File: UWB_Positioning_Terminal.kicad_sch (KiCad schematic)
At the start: 0 parts

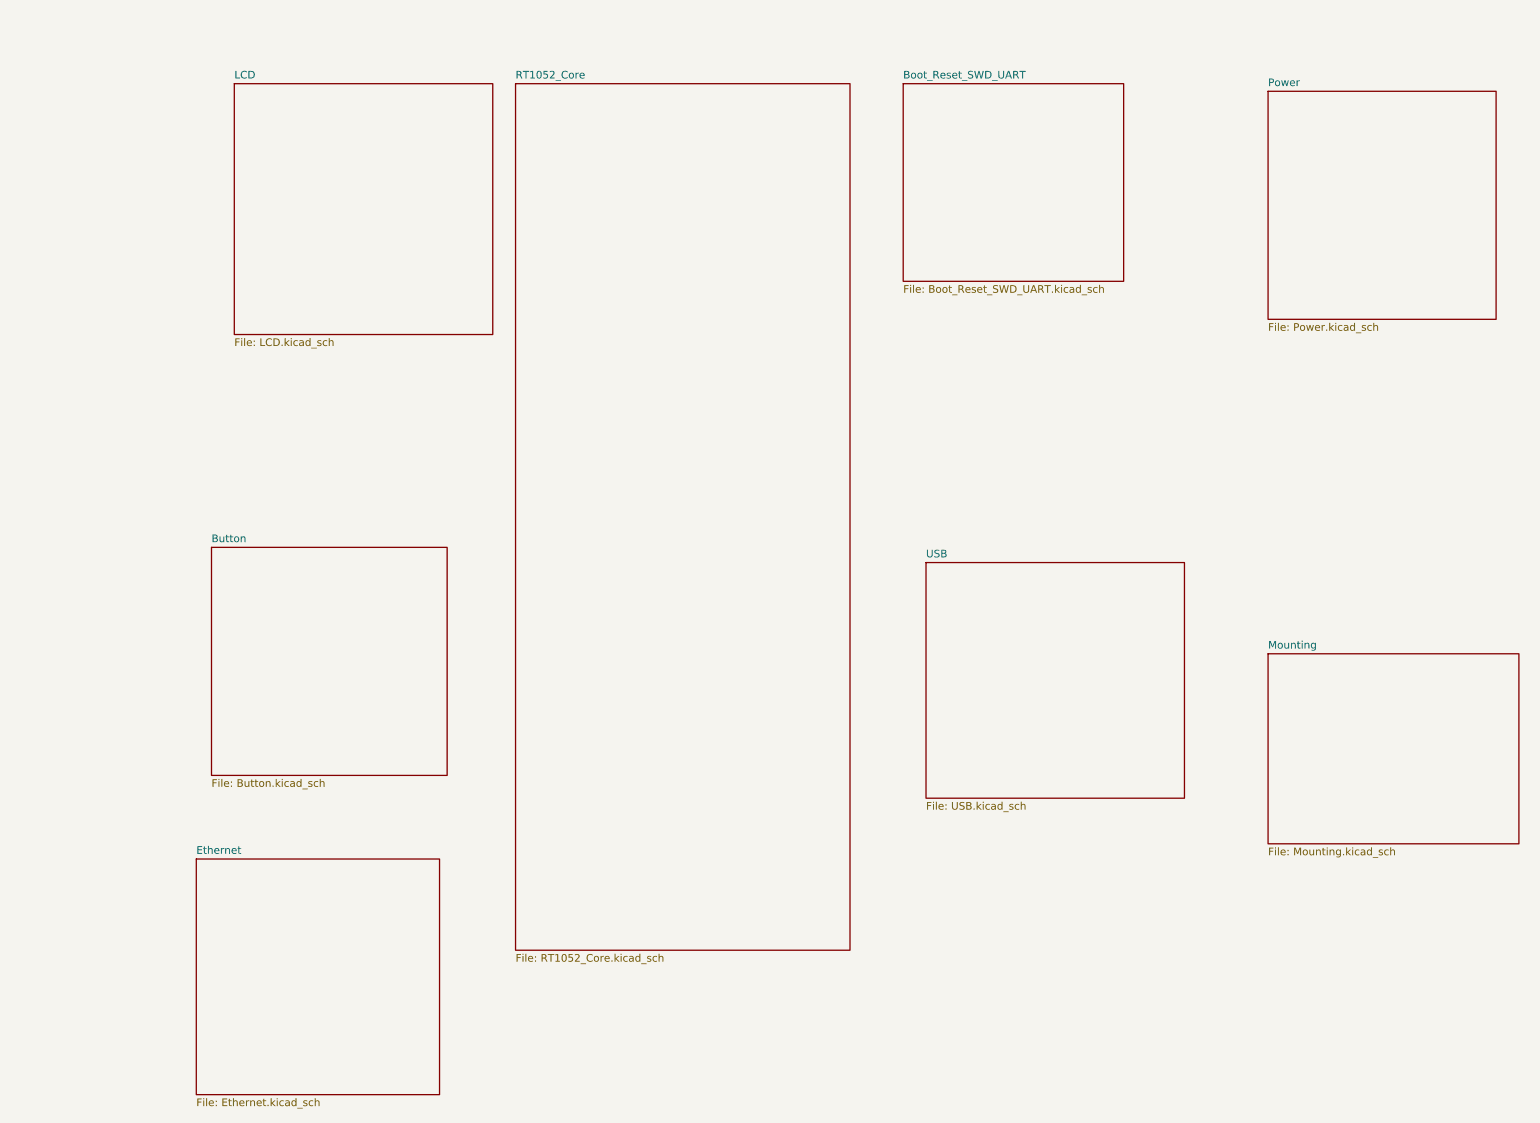
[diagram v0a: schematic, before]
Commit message: 2026 08 16 原理图完成，下一步制作分配未完成的器件封装，准备layout
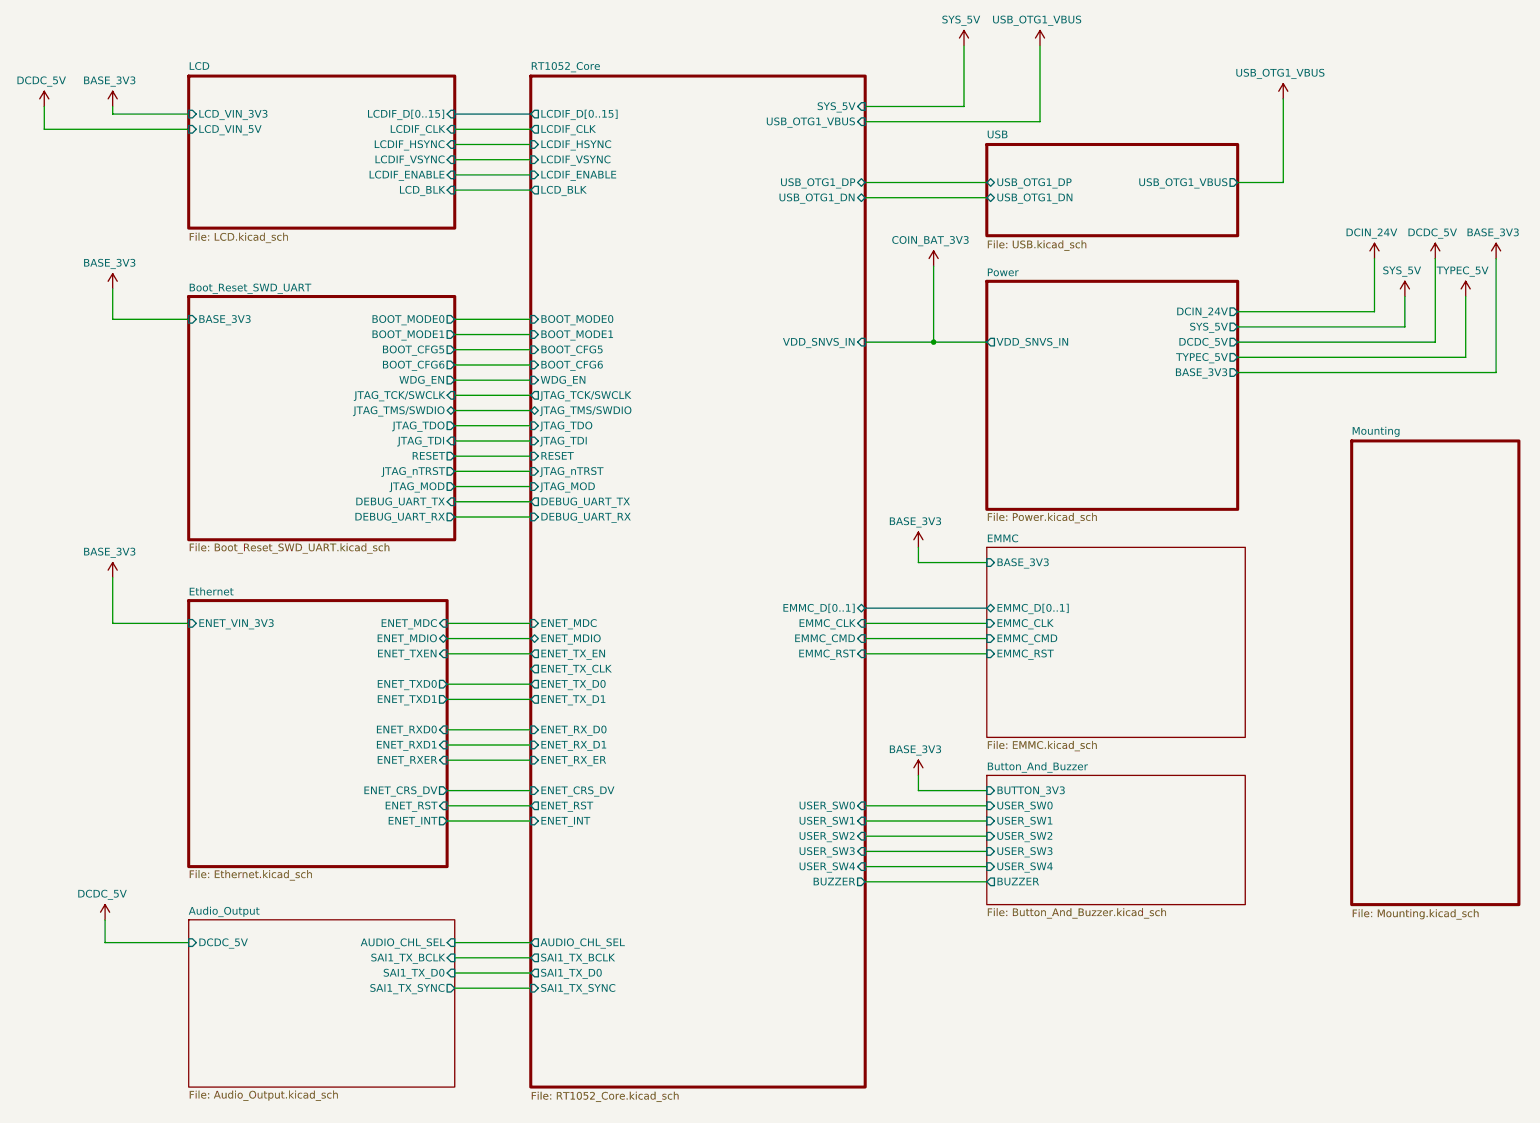
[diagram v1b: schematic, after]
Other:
- removed sheet Button
- added sheet Audio_Output (Audio_Output.kicad_sch)
- added sheet Button_And_Buzzer (Button_And_Buzzer.kicad_sch)
- added sheet EMMC (EMMC.kicad_sch)
- sheet Boot_Reset_SWD_UART ports: added BASE_3V3, BOOT_CFG5, BOOT_CFG6, BOOT_MODE0, BOOT_MODE1, DEBUG_UART_RX, DEBUG_UART_TX, JTAG_MOD, JTAG_TCK/SWCLK, JTAG_TDI, JTAG_TDO, JTAG_TMS/SWDIO, JTAG_nTRST, RESET, WDG_EN; removed none
- sheet Ethernet ports: added ENET_CRS_DV, ENET_INT, ENET_MDC, ENET_MDIO, ENET_RST, ENET_RXD0, ENET_RXD1, ENET_RXER, ENET_TXD0, ENET_TXD1, ENET_TXEN, ENET_VIN_3V3; removed none
- sheet LCD ports: added LCDIF_CLK, LCDIF_D[0..15], LCDIF_ENABLE, LCDIF_HSYNC, LCDIF_VSYNC, LCD_BLK, LCD_VIN_3V3, LCD_VIN_5V; removed none
- sheet Power ports: added BASE_3V3, DCDC_5V, DCIN_24V, SYS_5V, TYPEC_5V, VDD_SNVS_IN; removed none
- sheet RT1052_Core ports: added AUDIO_CHL_SEL, BOOT_CFG5, BOOT_CFG6, BOOT_MODE0, BOOT_MODE1, BUZZER, DEBUG_UART_RX, DEBUG_UART_TX, EMMC_CLK, EMMC_CMD, EMMC_D[0..1], EMMC_RST, ENET_CRS_DV, ENET_INT, ENET_MDC, ENET_MDIO, ENET_RST, ENET_RX_D0, ENET_RX_D1, ENET_RX_ER, ENET_TX_CLK, ENET_TX_D0, ENET_TX_D1, ENET_TX_EN, JTAG_MOD, JTAG_TCK/SWCLK, JTAG_TDI, JTAG_TDO, JTAG_TMS/SWDIO, JTAG_nTRST, LCDIF_CLK, LCDIF_D[0..15], LCDIF_ENABLE, LCDIF_HSYNC, LCDIF_VSYNC, LCD_BLK, RESET, SAI1_TX_BCLK, SAI1_TX_D0, SAI1_TX_SYNC, SYS_5V, USB_OTG1_DN, USB_OTG1_DP, USB_OTG1_VBUS, USER_SW0, USER_SW1, USER_SW2, USER_SW3, USER_SW4, VDD_SNVS_IN, WDG_EN; removed none
- sheet USB ports: added USB_OTG1_DN, USB_OTG1_DP, USB_OTG1_VBUS; removed none

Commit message: 2026 08 24 画图完成，准备生产
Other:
- sheet EMMC ports: added EMMC_3V3, EMMC_D[0..3]; removed BASE_3V3, EMMC_D[0..1]
- sheet Ethernet ports: added ENET_CLK; removed none
- sheet LCD ports: added LCD_RST; removed none
- sheet RT1052_Core ports: added EMMC_D[0..3], ENET_CLK, LCD_RST; removed EMMC_D[0..1], ENET_TX_CLK
